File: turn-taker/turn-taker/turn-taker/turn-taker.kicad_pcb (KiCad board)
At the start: 2 copper layers, 65.1 x 65.1 mm, 7 parts, among them J1 Conn_01x04_Pin, J2 Conn_01x04, SW1 SW_Push, SW2 SW_Push, SW3 SW_SPST

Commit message: generated gerber and drill files, v1
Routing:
- net GND: track 0.00 -> 146.2 mm
- net +5V: track 0.00 -> 45.5 mm
- net Net-(A1-GPIO15): track 0.00 -> 36.8 mm
- net Net-(J2-Pin_1): track 0.00 -> 25.6 mm
- net Net-(A1-GPIO14): track 0.00 -> 25.3 mm
- net BAT+: track 0.00 -> 11.7 mm
- net Net-(A1-GPIO4): track 0.00 -> 10.3 mm
- net Net-(A1-GPIO5): track 0.00 -> 9.46 mm
- added copper zone on B.Cu, net GND

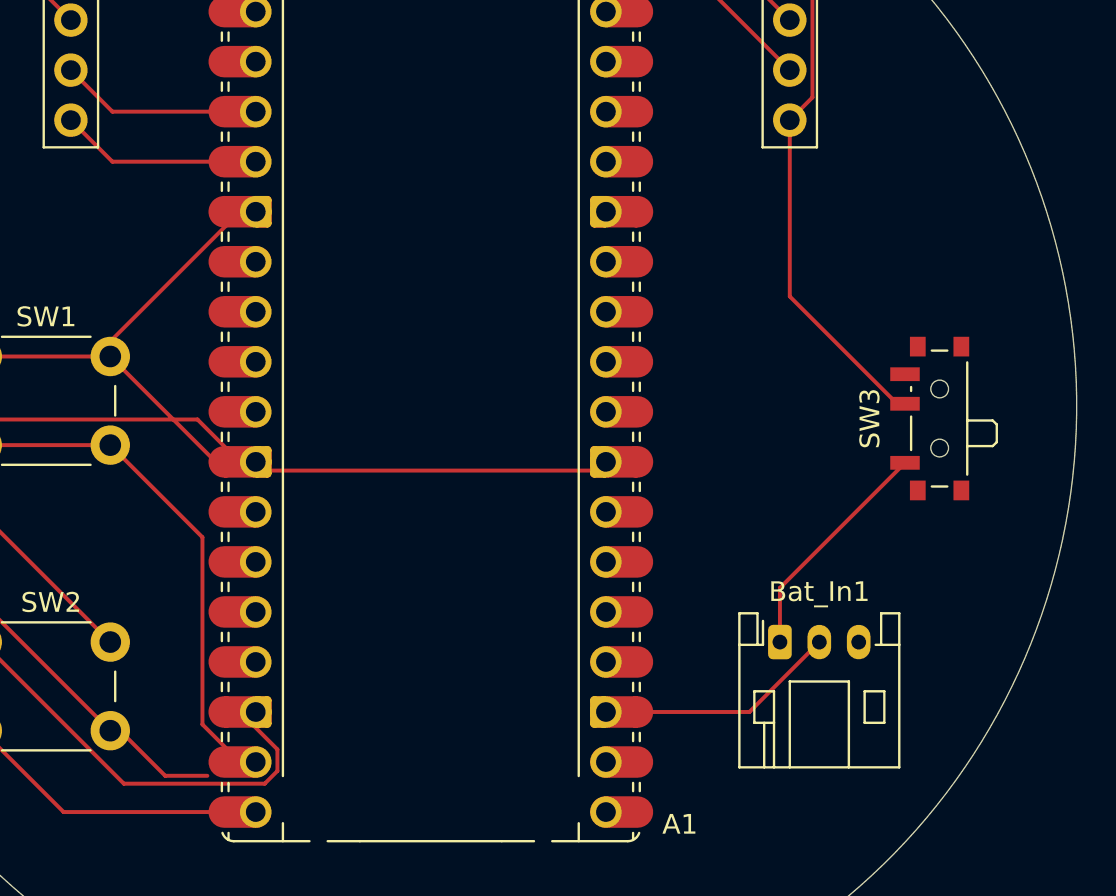
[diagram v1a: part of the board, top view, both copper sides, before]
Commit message: update pcb with correct switch footprint
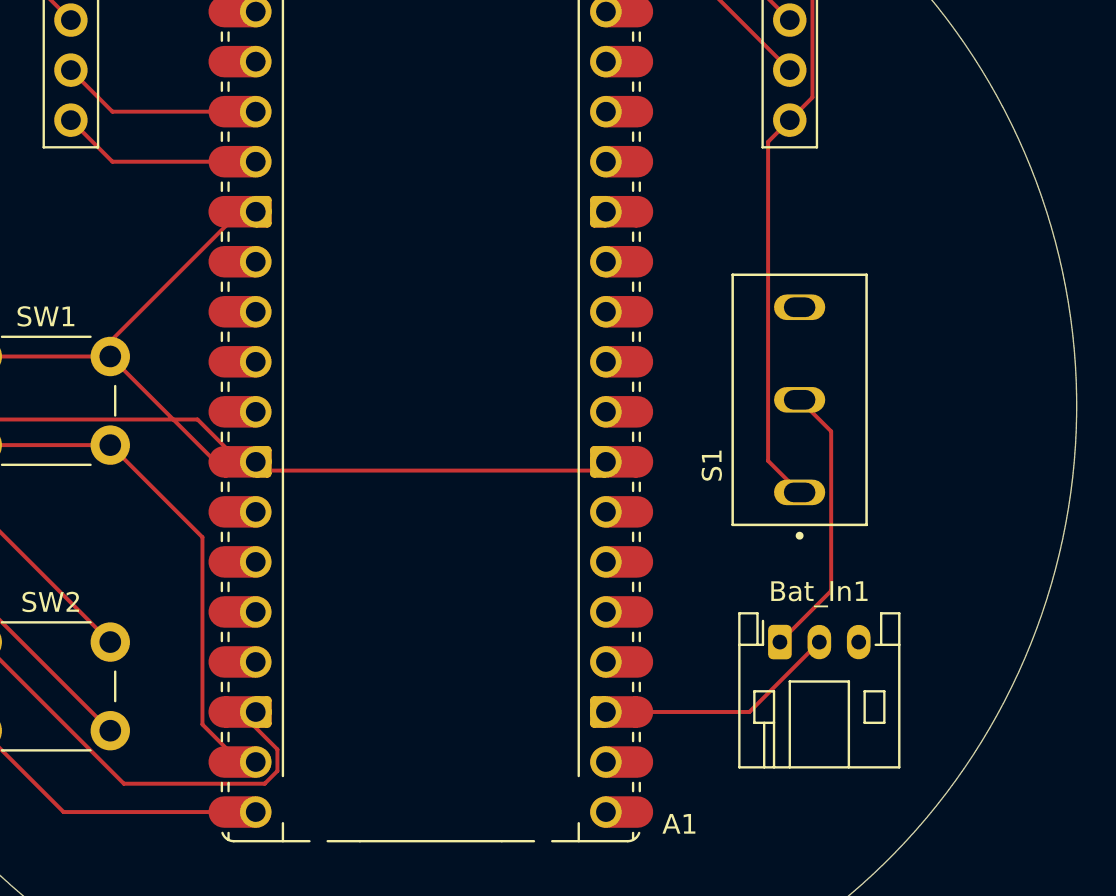
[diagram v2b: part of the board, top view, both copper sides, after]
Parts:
- removed SW3: SW_SPST, Button_Switch_SMD:SW_SPDT_PCM12
- added S1: SLW-1276864-4A-D, SLW_1276864_4A_D:SW_SLW-1276864-4A-D, F.Cu at (200.0, 86.2)
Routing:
- net Net-(A1-GPIO15): track 36.8 -> 31.4 mm
- net Net-(J2-Pin_1): track 25.6 -> 29.1 mm
- net BAT+: track 11.7 -> 14.0 mm

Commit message: update the jst connector for the screen in the schematic, footprint, and the pcb
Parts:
- J1: footprint Connector_PinHeader_2.54mm:PinHeader_1x04_P2.54mm_Vertical -> Connector_JST:JST_PH_B4B-PH-K_1x04_P2.00mm_Vertical
- moved J1 4.62 mm to (163.0, 69.0), turned to -90 degrees
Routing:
- net GND: track 146.2 -> 148.1 mm
- net Net-(A1-GPIO4): track 10.3 -> 9.18 mm
- net +5V: track 45.5 -> 46.6 mm
- net Net-(A1-GPIO5): track 9.46 -> 8.95 mm
